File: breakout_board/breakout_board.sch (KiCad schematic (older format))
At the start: 5 parts

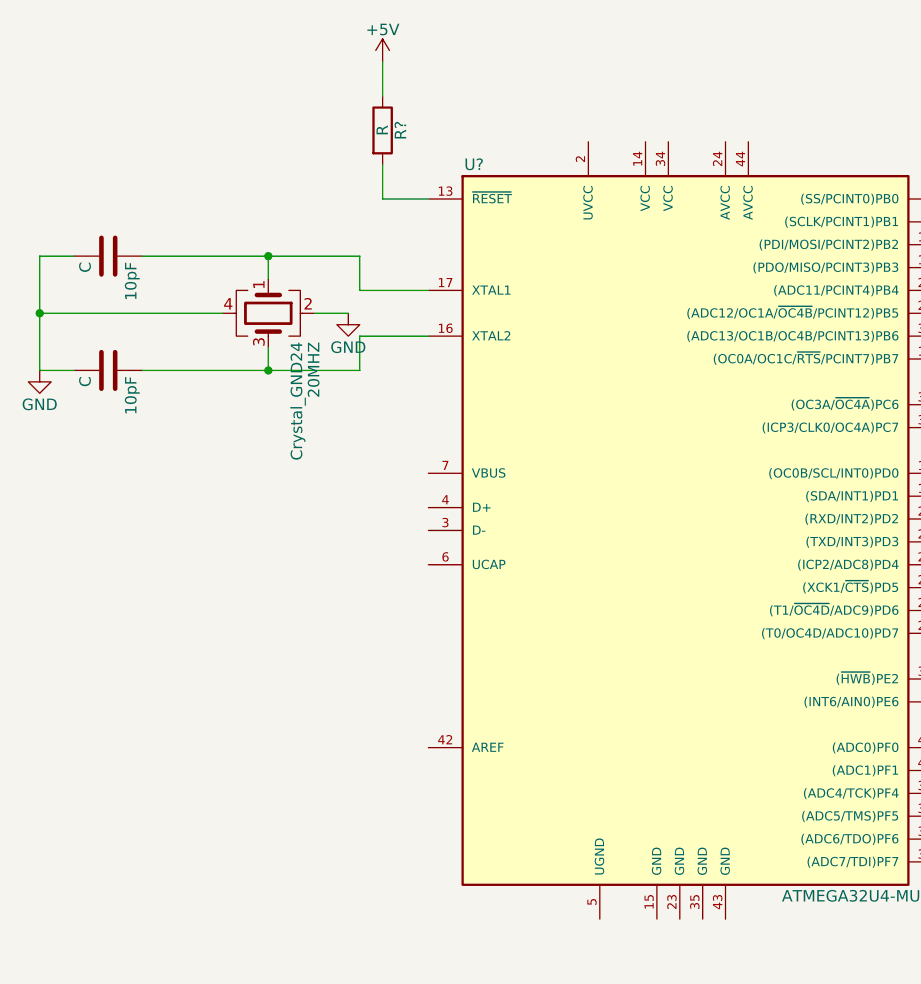
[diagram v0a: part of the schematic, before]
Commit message: Added some capacitors
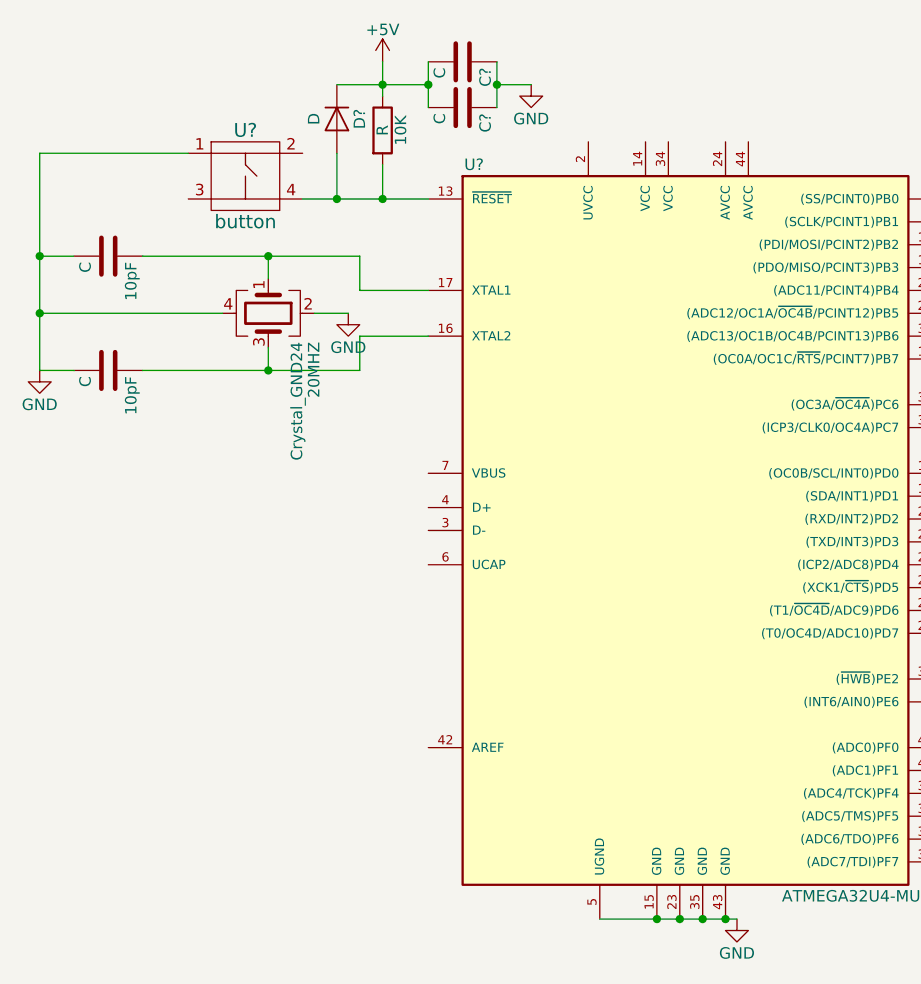
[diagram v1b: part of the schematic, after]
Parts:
- added C? (x2): C, symbol C
- added D?: D, symbol D
- added U?: button, symbol button
- gave numbers to parts that had none: 1
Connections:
- net +5V: now also C?.2, C?.2, D?.1 (K)
- net GND: now also U?.15 (GND), U?.23 (GND), U?.35 (GND), U?.43 (GND), U?.5 (UGND), C?.1, C?.1, U?.1
- net at 10K.2, U?.13 (~RESET~): now also D?.2 (A), U?.4
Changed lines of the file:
@@
 LIBS:valves
 LIBS:symbols
+LIBS:button
+LIBS:breakout_board-cache
 EELAYER 25 0
 EELAYER END
@@
 	0    1    1    0
 $EndComp
-Wire Wire Line
-	3850 2500 3550 2500
-Wire Wire Line
-	3550 2500 3550 2350
-Wire Wire Line
-	3550 2350 2600 2350
-Wire Wire Line
-	3850 2700 3550 2700
-Wire Wire Line
-	3550 2700 3550 2850
-Wire Wire Line
-	3550 2850 2600 2850
-Wire Wire Line
-	3150 2750 3150 2850
-Connection ~ 3150 2850
-Wire Wire Line
-	3150 2450 3150 2350
-Connection ~ 3150 2350
 $Comp
 L GND #PWR?
@@
 	1    0    0    -1
 $EndComp
-Wire Wire Line
-	2300 2850 2150 2850
-Wire Wire Line
-	2300 2350 2150 2350
-Wire Wire Line
-	2150 2350 2150 2850
-Wire Wire Line
-	2950 2600 2150 2600
-Connection ~ 2150 2600
 $Comp
 L GND #PWR?
@@
 	1    0    0    -1
 $EndComp
-Wire Wire Line
-	3350 2600 3500 2600
-$Comp
-L R R?
+$Comp
+L R 10K
 U 1 1 59CBE5AA
 P 3650 1800
-F 0 "R?" V 3730 1800 50  0000 C CNN
+F 0 "10K" V 3730 1800 50  0000 C CNN
 F 1 "R" V 3650 1800 50  0000 C CNN
 F 2 "" V 3580 1800 50  0001 C CNN
@@
 	1    0    0    -1
 $EndComp
-Wire Wire Line
-	3850 2100 3650 2100
+$Comp
+L button U?
+U 1 1 59CD35BF
+P 3050 2000
+F 0 "U?" H 3050 2200 60  0000 C CNN
+F 1 "button" H 3050 1800 60  0000 C CNN
+F 2 "" H 3050 2000 60  0001 C CNN
+F 3 "" H 3050 2000 60  0001 C CNN
+	1    3050 2000
+	1    0    0    -1
+$EndComp
+$Comp
+L D D?
+U 1 1 59CD3759
+P 3450 1750
+F 0 "D?" H 3450 1850 50  0000 C CNN
+F 1 "D" H 3450 1650 50  0000 C CNN
+F 2 "" H 3450 1750 50  0001 C CNN
+F 3 "" H 3450 1750 50  0001 C CNN
+	1    3450 1750
+	0    1    1    0
+$EndComp
+$Comp
+L C C?
+U 1 1 59CD37F8
+P 4000 1500
+F 0 "C?" H 4025 1600 50  0000 L CNN
+F 1 "C" H 4025 1400 50  0000 L CNN
+F 2 "" H 4038 1350 50  0001 C CNN
+F 3 "" H 4000 1500 50  0001 C CNN
+	1    4000 1500
+	0    1    1    0
+$EndComp
+$Comp
+L C C?
+U 1 1 59CD3865
+P 4000 1700
+F 0 "C?" H 4025 1800 50  0000 L CNN
+F 1 "C" H 4025 1600 50  0000 L CNN
+F 2 "" H 4038 1550 50  0001 C CNN
+F 3 "" H 4000 1700 50  0001 C CNN
+	1    4000 1700
+	0    1    1    0
+$EndComp
+$Comp
+L GND #PWR?
+U 1 1 59CD3971
+P 4300 1600
+F 0 "#PWR?" H 4300 1350 50  0001 C CNN
+F 1 "GND" H 4300 1450 50  0000 C CNN
+F 2 "" H 4300 1600 50  0001 C CNN
+F 3 "" H 4300 1600 50  0001 C CNN
+	1    4300 1600
+	1    0    0    -1
+$EndComp
+Wire Wire Line
+	3850 2500 3550 2500
+Wire Wire Line
+	3550 2500 3550 2350
+Wire Wire Line
+	3550 2350 2600 2350
+Wire Wire Line
+	3850 2700 3550 2700
+Wire Wire Line
+	3550 2700 3550 2850
+Wire Wire Line
+	3550 2850 2600 2850
+Wire Wire Line
+	3150 2750 3150 2850
+Connection ~ 3150 2850
+Wire Wire Line
+	3150 2450 3150 2350
+Connection ~ 3150 2350
+Wire Wire Line
+	2150 2850 2300 2850
+Wire Wire Line
+	2300 2350 2150 2350
+Wire Wire Line
+	2150 1900 2150 2850
+Wire Wire Line
+	2950 2600 2150 2600
+Connection ~ 2150 2600
+Wire Wire Line
+	3350 2600 3500 2600
+Wire Wire Line
+	3300 2100 3850 2100
 Wire Wire Line
 	3650 2100 3650 1950
 Wire Wire Line
 	3650 1650 3650 1500
+Connection ~ 3650 2100
+Wire Wire Line
+	2800 1900 2150 1900
+Connection ~ 2150 2350
+Wire Wire Line
+	3450 1900 3450 2100
+Connection ~ 3450 2100
+Wire Wire Line
+	3450 1600 3850 1600
+Connection ~ 3650 1600
+Wire Wire Line
+	3850 1500 3850 1700
+Connection ~ 3850 1600
+Wire Wire Line
+	4150 1500 4150 1700
+Wire Wire Line
+	4150 1600 4300 1600
+Connection ~ 4150 1600
+Wire Wire Line
+	4600 5250 5200 5250
+Connection ~ 4850 5250
+Connection ~ 4950 5250
+Connection ~ 5050 5250
+$Comp
+L GND #PWR?
+U 1 1 59CD422B
+P 5200 5250
+F 0 "#PWR?" H 5200 5000 50  0001 C CNN
+F 1 "GND" H 5200 5100 50  0000 C CNN
+F 2 "" H 5200 5250 50  0001 C CNN
+F 3 "" H 5200 5250 50  0001 C CNN
+	1    5200 5250
+	1    0    0    -1
+$EndComp
+Connection ~ 5150 5250
 $EndSCHEMATC

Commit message: Added IMU
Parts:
- added 100nF (x2), 1uF (x3): C, symbol C
- added 10K (x2), 10k (x8), 1K (x4), 200k: R, symbol R
- added 10uF (x2): CP, symbol CP
- added 30±25%ohm: Ferrite_Bead, symbol Ferrite_Bead
- added BS170 (x2): Q_NMOS_DGS, symbol Q_NMOS_DGS
- added ICSP: CONN_02X03, symbol CONN_02X03
- added J? (x2): CONN_01X17, symbol CONN_01X17
- added L, ON, RX, TX: LED, symbol LED
- added LSM6DS3US: IMU, symbol IMU
- added U?: Level_Shifter_4Channel, symbol Level_Shifter_4Channel
- added V_REG: NCP1117-5, symbol NCP1117-5
- added V_REG_1V8: NCP1117DT18RKG, symbol NCP1117-5
- gave numbers to parts that had none: 3
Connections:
- net +5V: now also U?.14 (VCC), U?.2 (UVCC), U?.24 (AVCC), U?.34 (VCC), 10k.1, 10k.1, 10k.2, 10k.2, 10uF.1, 1K.2, 200k.1, 30±25%ohm.1, ICSP.2 (P2), J?.6 (P6), V_REG.2, V_REG.4, V_REG_1V8.3
- net GND: now also U?.7 (VBUS), 100nF.2, 100nF.2, 10K.1, 10uF.2, 10uF.2, 1uF.2, 1uF.2, 1uF.2, ICSP.6 (P6), J?.4 (P4), J?.6 (P6), L.1 (K), LSM6DS3US.2 (SDx), LSM6DS3US.3 (SCx), LSM6DS3US.6 (GND), LSM6DS3US.7 (GND), ON.1 (K), RX.1 (K), TX.1 (K), U?.6 (GND), V_REG.1, V_REG_1V8.1
- net D7: now reaches U?.1 ((INT6/AIN0)PE6)
- net D7: now also J?.12 (P12)
- net MOSI: now reaches U?.10 ((PDI/MOSI/PCINT2)PB2)
- net MOSI: now also ICSP.4 (P4), J?.1 (P1)
- net MISO: now reaches U?.11 ((PDO/MISO/PCINT3)PB3)
- net MISO: now also ICSP.1 (P1), J?.2 (P2)
- net IO11*: now reaches U?.12 ((OC0A/OC1C/~RTS~/PCINT7)PB7)
- net IO11*: now also J?.16 (P16)
- net RESET: now reaches 10K.2, CD1206-S01575.2 (A), CKN10291CT-ND.4, U?.13 (~RESET~)
- net RESET: now also ICSP.5 (P5), J?.5 (P5), J?.5 (P5)
- net D3/SCL: now reaches U?.18 ((OC0B/SCL/INT0)PD0)
- net D3/SCL: now also 10k.1, J?.8 (P8), U?.10 (B1)
- net D2/SDA: now reaches U?.19 ((SDA/INT1)PD1)
- net D2/SDA: now also 10k.1, J?.7 (P7), U?.9 (B2)
- net D0/RX: now reaches U?.20 ((RXD/INT2)PD2)
- net D0/RX: now also J?.4 (P4)
- net D1/TX: now reaches U?.21 ((TXD/INT3)PD3)
- net D1/TX: now also J?.3 (P3)
- net TXLED: now reaches U?.22 ((XCK1/~CTS~)PD5)
- net TXLED: now also 1K.2
- net D4*: now reaches U?.25 ((ICP2/ADC8)PD4)
- net D4*: now also J?.9 (P9), U?.8 (B3)
- net IO12*: now reaches U?.26 ((T1/~OC4D~/ADC9)PD6)
- net IO12*: now also J?.17 (P17)
- net D6*: now reaches U?.27 ((T0/OC4D/ADC10)PD7)
- net D6*: now also J?.11 (P11)
- net IO8: now reaches U?.28 ((ADC11/PCINT4)PB4)
- net IO8: now also J?.13 (P13)
- net IO9*: now reaches U?.29 ((ADC12/OC1A/~OC4B~/PCINT12)PB5)
- net IO9*: now also J?.14 (P14)
- net IO10*: now reaches U?.30 ((ADC13/OC1B/OC4B/PCINT13)PB6)
- net IO10*: now also J?.15 (P15)
- net D5*: now reaches U?.31 ((OC3A/~OC4A~)PC6)
- net D5*: now also J?.10 (P10), U?.7 (B4)
- net IO13*: now reaches U?.32 ((ICP3/CLK0/OC4A)PC7)
- net IO13*: now also 1K.2, J?.17 (P17)
- net HWB: now reaches U?.33 ((~HWB~)PE2)
- net HWB: now also 10K.2
- net A0: now reaches U?.36 ((ADC7/TDI)PF7)
- net A0: now also J?.14 (P14)
- net A1: now reaches U?.37 ((ADC6/TDO)PF6)
- net A1: now also J?.13 (P13)
- net A2: now reaches U?.38 ((ADC5/TMS)PF5)
- net A2: now also J?.12 (P12)
- net A3: now reaches U?.39 ((ADC4/TCK)PF4)
- net A3: now also J?.11 (P11)
- net A4: now reaches U?.40 ((ADC1)PF1)
- net A4: now also J?.10 (P10)
- net A5: now reaches U?.41 ((ADC0)PF0)
- net A5: now also J?.9 (P9)
- net AREF: now reaches U?.42 (AREF)
- net AREF: now also 100nF.1, J?.15 (P15)
- net at U?.44 (AVCC): now also 1uF.1, 30±25%ohm.2
- net at U?.6 (UCAP): now also 1uF.1
- net RXLED/SS: now reaches U?.8 ((SS/PCINT0)PB0)
- net RXLED/SS: now also 1K.2, J?.2 (P2)
- net SCK: now reaches U?.9 ((SCLK/PCINT1)PB1)
- net SCK: now also ICSP.3 (P3), J?.1 (P1)
- new net: 1K.1, RX.2 (A)
- new net: 1K.1, L.2 (A)
- new net: 1K.1, TX.2 (A)
- new net: 1K.1, ON.2 (A)
- new net: 200k.2, U?.11 (Vref_B), U?.12 (EN)
- new net +12V: 10uF.1, J?.3 (P3), V_REG.3
- new net +1V8: 100nF.1, 10K.2, 10k.1, 10k.1, 10k.2, 10k.2, 1uF.1, BS170.2 (G), BS170.2 (G), LSM6DS3US.5 (VDDIO), LSM6DS3US.8 (VDD), U?.1 (Vref_A), V_REG_1V8.2, V_REG_1V8.4
- new net INT1: LSM6DS3US.4 (INT1), U?.4 (A3)
- new net INT2: LSM6DS3US.9 (INT2), U?.5 (A4)
- new net L_HI: 10K.1, LSM6DS3US.1 (SDO/SA0), LSM6DS3US.12 (CS)
- new net SCL_1V8: 10k.1, 10k.2, BS170.3 (S), LSM6DS3US.13 (SCL), U?.2 (A1)
- new net SCL_5V: 10k.2, BS170.1 (D)
- new net SDA_1V8: 10k.1, 10k.2, BS170.3 (S), LSM6DS3US.14 (SDA), U?.3 (A2)
- new net SDA_5V: 10k.2, BS170.1 (D)
- no-connect marks 0 -> 7
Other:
- note added: "blue"
- note added: "green"
- note added: "yellow"
- moved on the sheet: 100nF, 10K, 10pF, 20MHZ, CD1206-S01575, CKN10291CT-ND, U?

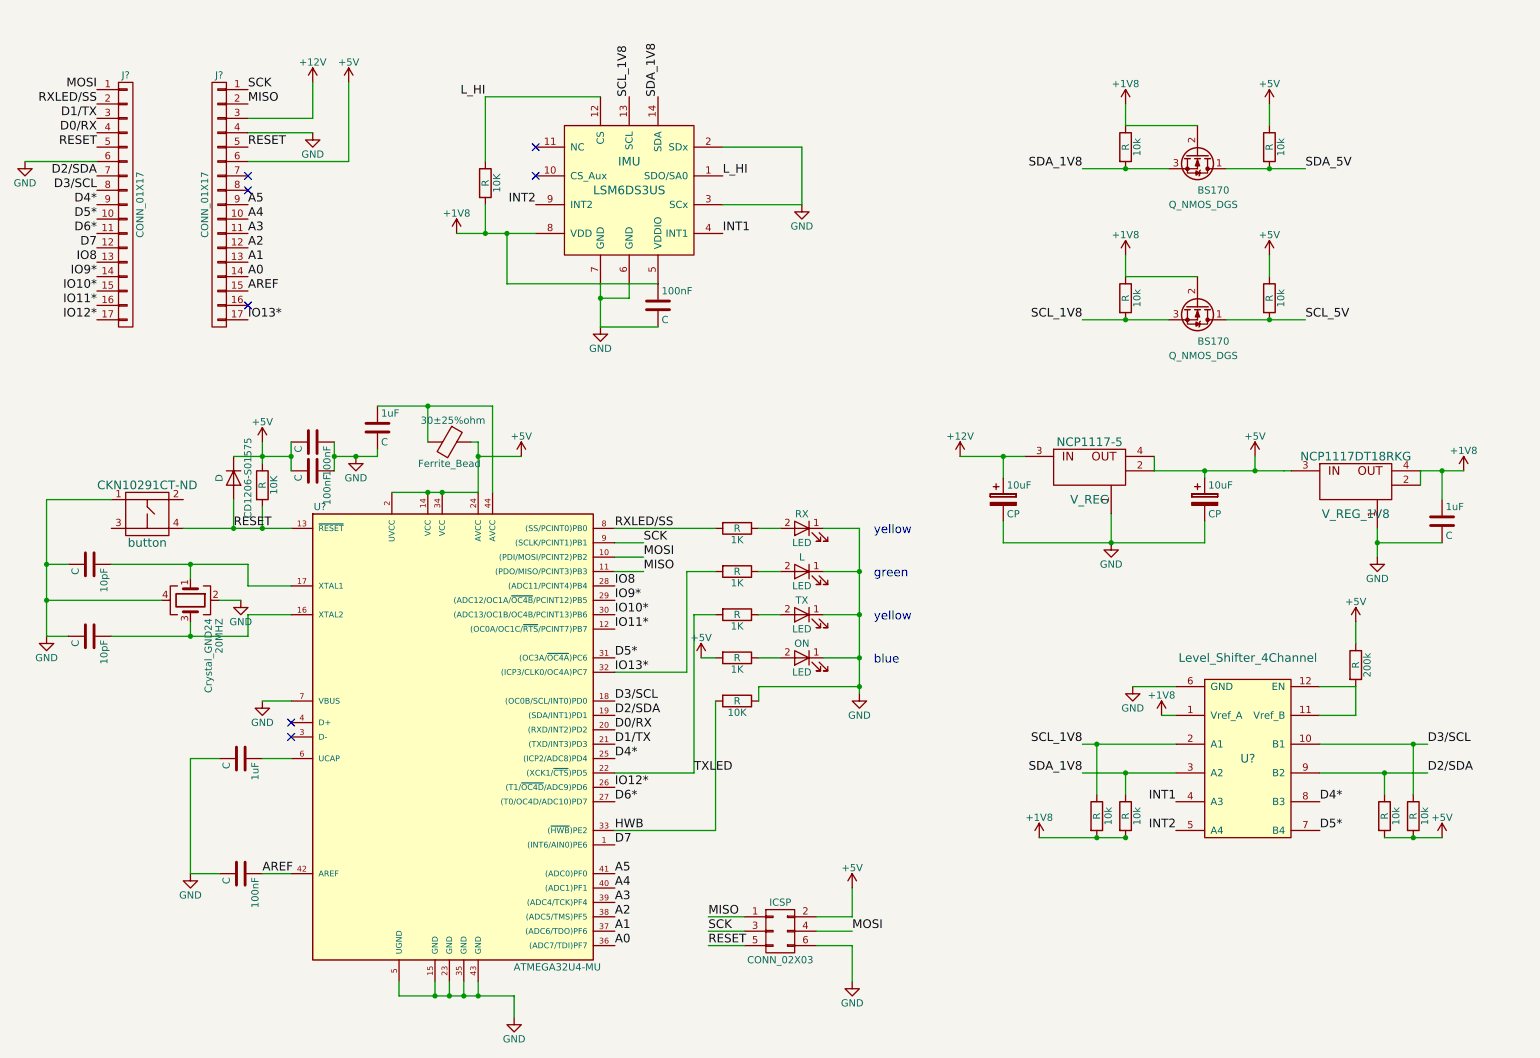
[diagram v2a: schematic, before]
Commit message: Added brushed motor driver and headers
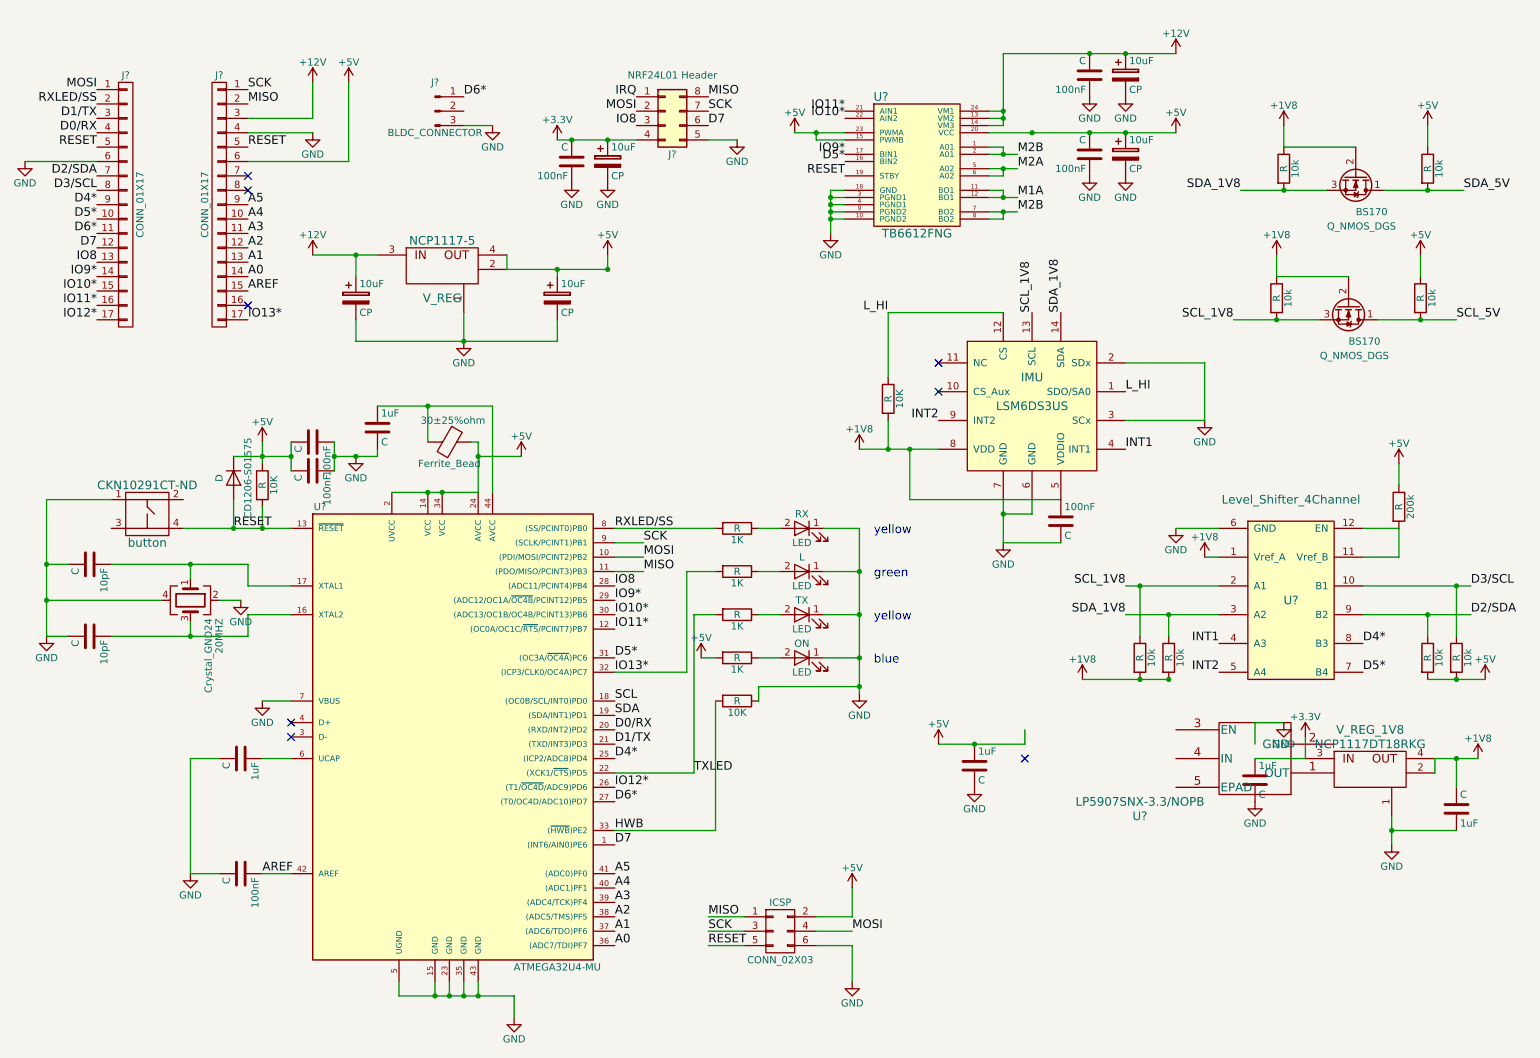
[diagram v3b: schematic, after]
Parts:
- added 100nF (x3), 1uF (x2): C, symbol C
- added 10uF (x3): CP, symbol CP
- added J?: BLDC_CONNECTOR, Connectors:PINHEAD1-3, symbol Conn_01x03_Male
- added J?: NRF24L01 Header, symbol Conn_02x04_Counter_Clockwise
- added U?: TB6612FNG, symbol TB6612FNG
- added U?: LP5907SNX-3.3/NOPB, DQN4, symbol LP5907SNX-3.3/NOPB
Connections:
- net +12V: now also 100nF.2, 10uF.1, U?.13 (VM2), U?.14 (VM3), U?.24 (VM1)
- net +1V8: now also 1uF.2; no longer 1uF.1
- net +5V: now also 100nF.2, 10uF.1, 1uF.1, U?.15 (PWMB), U?.20 (VCC), U?.23 (PWMA); no longer V_REG_1V8.3
- net D2/SDA: no longer U?.19 ((SDA/INT1)PD1)
- net D3/SCL: no longer U?.18 ((OC0B/SCL/INT0)PD0)
- net D5*: now also U?.16 (BIN2)
- net D6*: now also J?.1 (Pin_1)
- net D7: now also J?.6 (Pin_6)
- net GND: now also 1uF.1, 100nF.1, 100nF.1, 100nF.1, 10uF.2, 10uF.2, 10uF.2, 1uF.2, 1uF.2, J?.3 (Pin_3), J?.5 (Pin_5), U?.10 (PGND2), U?.18 (GND), U?.3 (PGND1), U?.4 (PGND1), U?.9 (PGND2); no longer 1uF.2
- net IO10*: now also U?.22 (AIN2)
- net IO11*: now also U?.21 (AIN1)
- net IO8: now also J?.3 (Pin_3)
- net IO9*: now also U?.17 (BIN1)
- net MISO: now also J?.8 (Pin_8)
- net MOSI: now also J?.2 (Pin_2)
- net RESET: now also U?.19 (STBY)
- net SCK: now also J?.7 (Pin_7)
- new net +3V3: 100nF.2, 10uF.1, 1uF.1, J?.4 (Pin_4), V_REG_1V8.3
- new net IRQ: J?.1 (Pin_1)
- new net M1A: U?.11 (BO1), U?.12 (BO1)
- new net M2A: U?.5 (A02), U?.6 (A02)
- new net M2B: U?.1 (A01), U?.2 (A01), U?.7 (BO2), U?.8 (BO2)
- new net SCL: U?.18 ((OC0B/SCL/INT0)PD0)
- new net SDA: U?.19 ((SDA/INT1)PD1)
- no-connect marks 7 -> 8
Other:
- moved on the sheet: 100nF, 10K, 10k, 10uF, 1uF, 200k, BS170, LSM6DS3US, U?, V_REG, V_REG_1V8
